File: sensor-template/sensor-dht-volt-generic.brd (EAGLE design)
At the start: 22.1 x 27.3 mm, 19 parts, among them U2 ATMEGA328PB-AUR

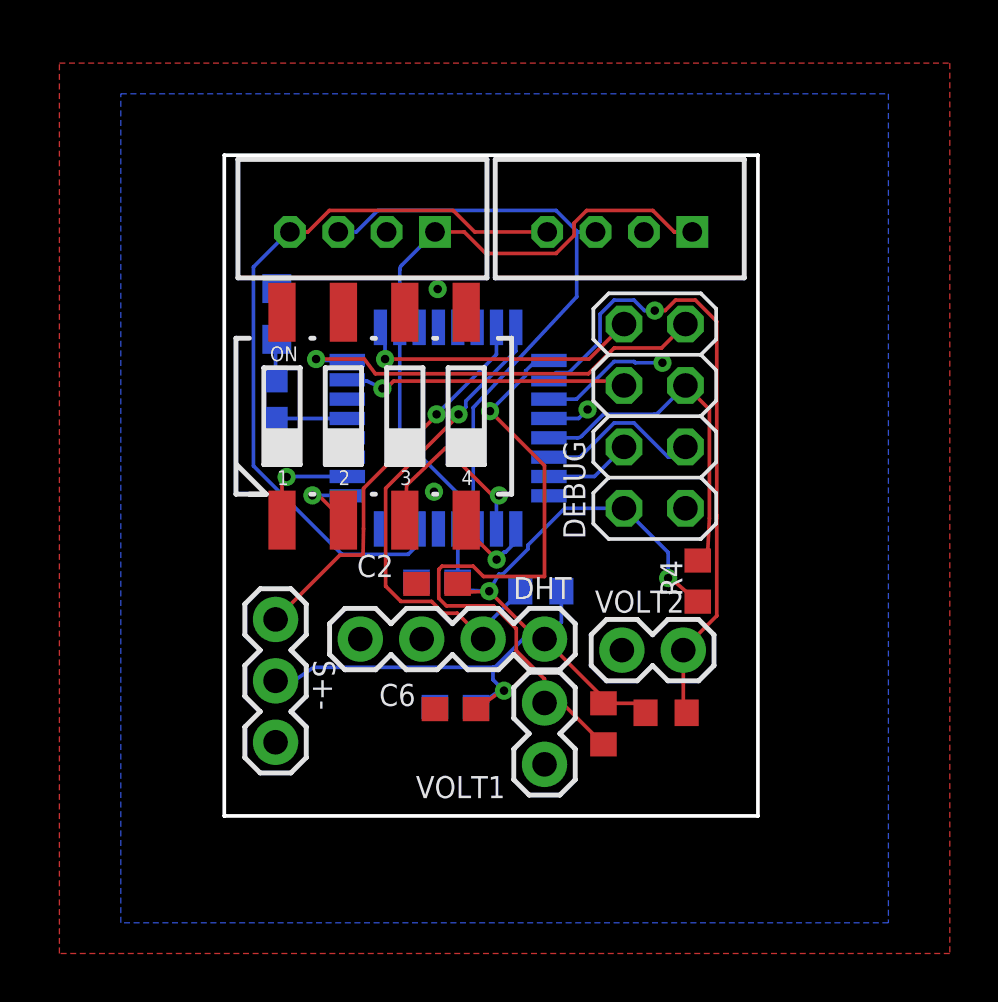
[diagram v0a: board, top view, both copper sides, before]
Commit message: Optional pullup on I2C + Default I2C0
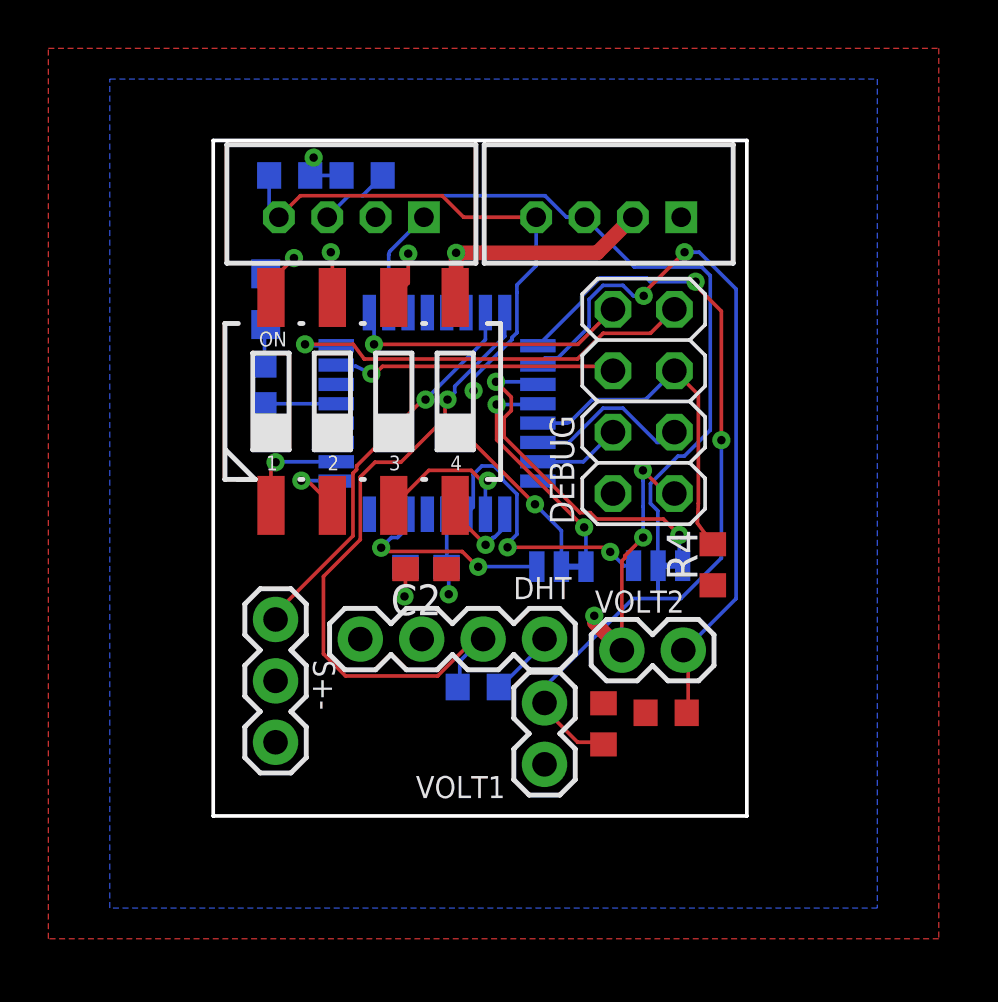
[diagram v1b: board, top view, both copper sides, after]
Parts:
- removed C5: 10u, resistor:C0603
- removed C6: 0.1u, resistor:C0603
- added J_SCL: SCL_Select, SparkFun-Jumpers:SMT-JUMPER_3_1-NC_TRACE_SILK
- added J_SDA: SDA_Select, SparkFun-Jumpers:SMT-JUMPER_3_1-NC_TRACE_SILK
- added R6, R7: 10k, resistor:R0603
- moved R1 4.73 mm to (11.0, 5.94)
- moved R4 0.92 mm to (20.7, 11.0)
- moved C1 0.76 mm to (8.81, 10.9)
- moved DEBUG 0.76 mm to (17.8, 17.8)
- moved R5 0.76 mm to (2.13, 18.4)
- moved S2 0.76 mm to (6.21, 17.8)
- moved U$3 0.76 mm to (16.4, 25.4)
- moved U$4 0.76 mm to (5.73, 25.4)
- moved LED1 0.76 mm to (2.18, 22.0)
- moved U2 0.76 mm to (9.27, 17.3)
- moved C2 0.76 mm to (8.81, 10.8)
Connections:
- new net SCL: J_SCL.2, R6.2, U$3.4, U$4.4
- new net SDA: J_SDA.2, R7.2, U$3.3, U$4.3
- net SCL0: now also J_SCL.3
- net SCL1: now also J_SCL.1; no longer U$3.4, U$4.4
- net SDA0: now also J_SDA.3
- net SDA1: now also J_SDA.1; no longer U$3.3, U$4.3
- net VCC: now also R6.1, R7.1; no longer C5.1, C6.1
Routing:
- net VCC: track 70.8 -> 12.8 mm, vias 3 -> 2
- net SDA: track 0.00 -> 34.1 mm
- net SCL: track 0.00 -> 30.3 mm, vias 0 -> 2
- net GND: track 0.00 -> 28.3 mm, vias 2 -> 8
- net SCL1: track 30.9 -> 8.77 mm, vias 0 -> 2
- net SDA1: track 25.4 -> 12.2 mm, vias 0 -> 2
- net SDA0: track 5.36 -> 14.5 mm, vias 1 -> 2
- net SCL0: track 1.75 -> 9.96 mm, vias 1 -> 2
- net A1: track 20.5 -> 28.0 mm
- net A2: track 27.5 -> 33.3 mm, vias 1 -> 2
- net A3: track 26.5 -> 30.5 mm, vias 1 -> 2
- net N$2: track 8.12 -> 6.10 mm
- added copper zone on layer 1, net VCC
- removed copper zone on layer 1, net GND
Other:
- board size 22.1 x 27.3 mm -> 22.1 x 27.9 mm

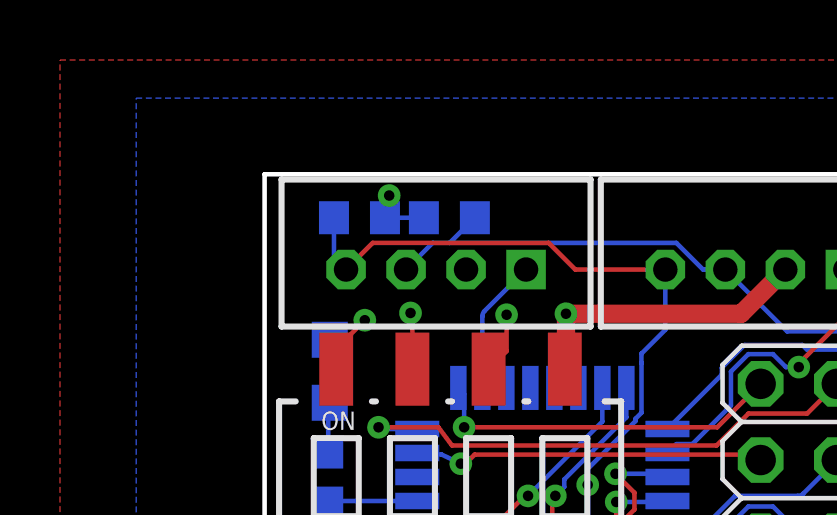
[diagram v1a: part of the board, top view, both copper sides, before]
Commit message: Post-ramp circuit fixes
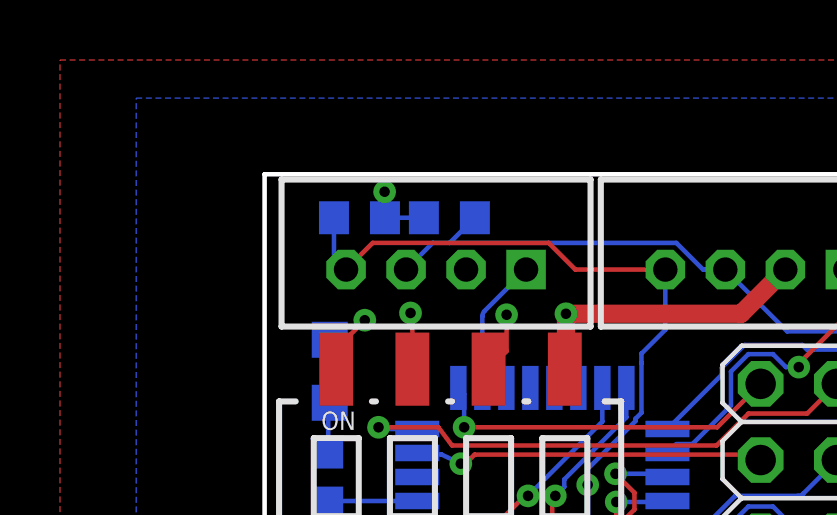
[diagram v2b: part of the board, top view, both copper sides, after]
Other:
- board text added: "DHT+Analog v0.3"
- board text removed: "DHT+Analog v0.1"
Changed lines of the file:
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@@
 <text x="21.336" y="26.2128" size="0.9144" layer="26" rot="MR0">WaggleNet Sensor</text>
 <text x="21.1836" y="23.0124" size="0.6096" layer="26" distance="30" rot="MR0">(c) Sunmola Oreoluwa, Jimmy He</text>
-<text x="9.4488" y="26.2128" size="0.6096" layer="26" rot="MR0">DHT+Analog v0.1</text>
+<text x="9.4488" y="26.2128" size="0.6096" layer="26" rot="MR0">DHT+Analog v0.3</text>
 <wire x1="0.0127" y1="0.6096" x2="0.0127" y2="28.5496" width="0.1524" layer="20"/>
 <wire x1="0.0127" y1="28.5496" x2="22.0853" y2="28.5496" width="0.1524" layer="20"/>
@@
 <param name="mdViaViaSameLayer" value="6mil"/>
 <param name="mnLayersViaInSmd" value="2"/>
-<param name="mdCopperDimension" value="10mil"/>
+<param name="mdCopperDimension" value="5mil"/>
 <param name="mdDrill" value="6mil"/>
 <param name="mdSmdStop" value="0mil"/>
@@
 <param name="mlMinCreamFrame" value="0mil"/>
 <param name="mlMaxCreamFrame" value="0mil"/>
-<param name="mlViaStopLimit" value="0mil"/>
+<param name="mlViaStopLimit" value="20mil"/>
 <param name="srRoundness" value="0"/>
 <param name="srMinRoundness" value="0mil"/>
@@
 <contactref element="R7" pad="1"/>
 <wire x1="4.025" y1="27.1018" x2="5.3222" y2="27.1018" width="0.1524" layer="16"/>
-<wire x1="4.025" y1="27.1018" x2="4.025" y2="27.7006" width="0.1524" layer="16"/>
-<wire x1="4.025" y1="27.7006" x2="4.1656" y2="27.8412" width="0.1524" layer="16"/>
-<via x="4.1656" y="27.8412" extent="1-16" drill="0.35"/>
+<wire x1="4.025" y1="27.1018" x2="4.025" y2="27.9564" width="0.1524" layer="16"/>
+<wire x1="4.025" y1="27.9564" x2="4.0132" y2="27.9682" width="0.1524" layer="16"/>
+<via x="4.0132" y="27.9682" extent="1-16" drill="0.35"/>
 </signal>
 <signal name="A3">
